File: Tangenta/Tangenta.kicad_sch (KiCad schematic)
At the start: 9 parts

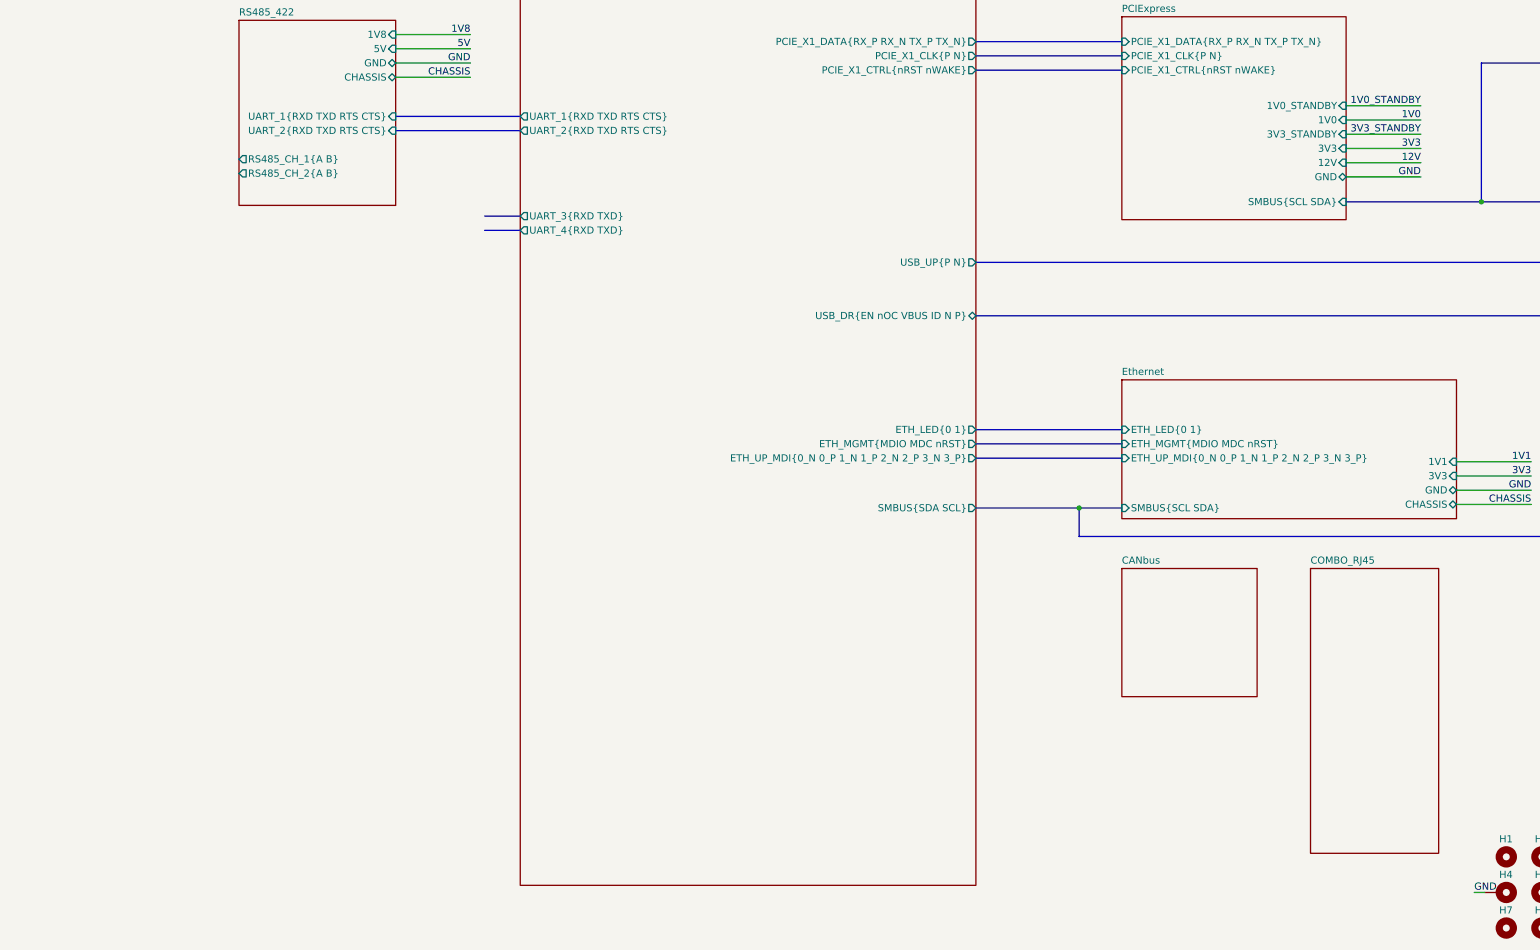
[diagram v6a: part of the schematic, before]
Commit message: Dual RS485 routed, done.
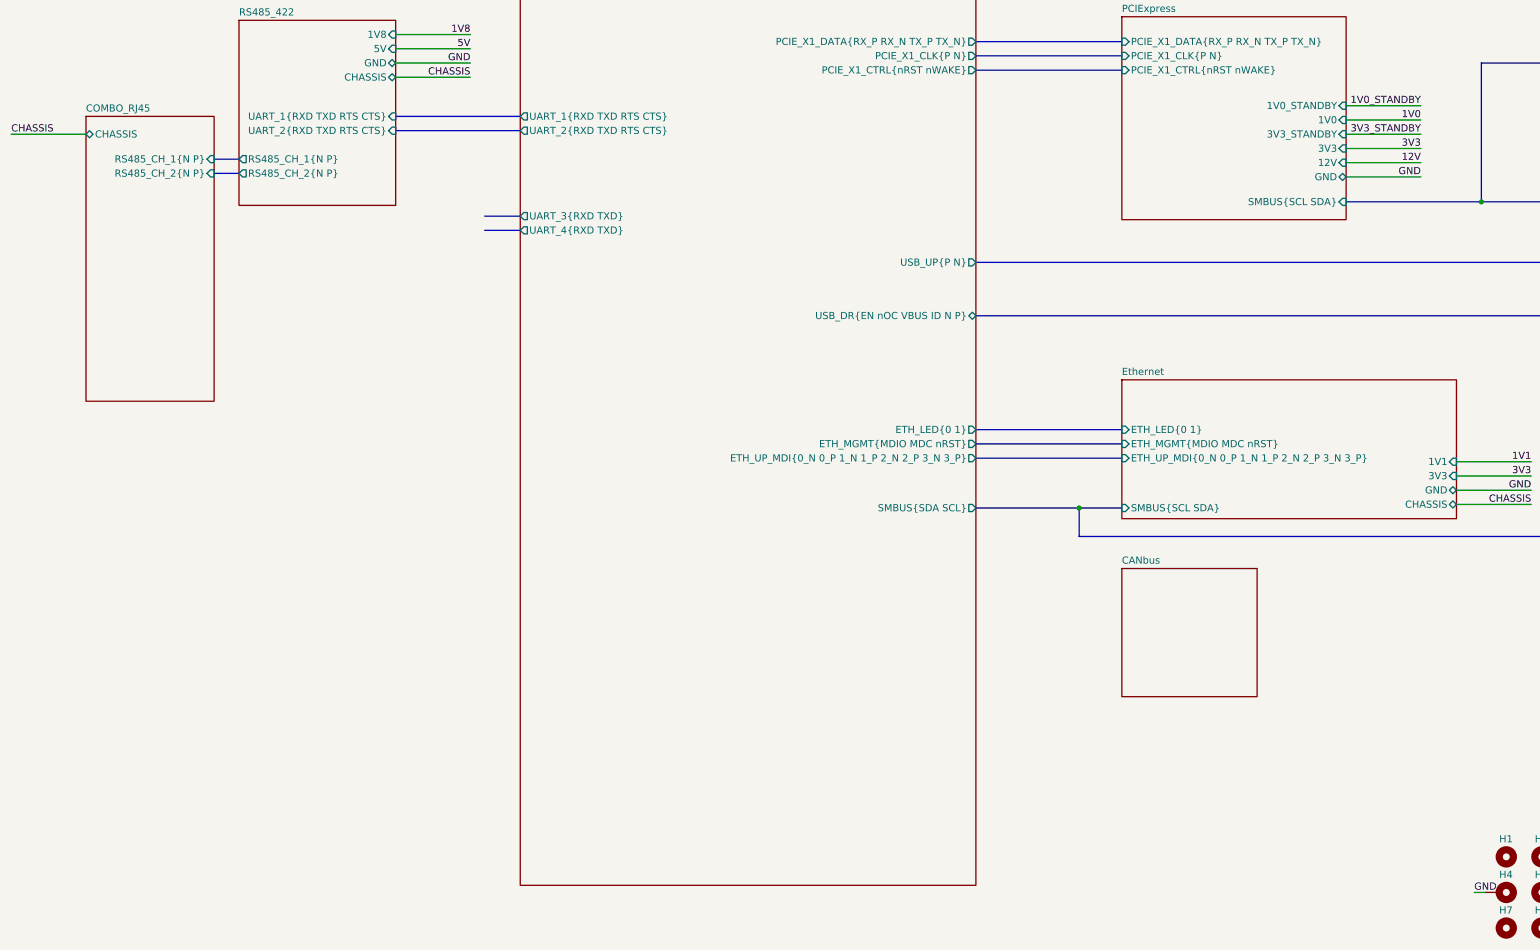
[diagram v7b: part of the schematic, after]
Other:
- sheet COMBO_RJ45 ports: added CHASSIS, RS485_CH_1{N P}, RS485_CH_2{N P}; removed none
- sheet RS485_422 ports: added RS485_CH_1{N P}, RS485_CH_2{N P}; removed RS485_CH_1{A B}, RS485_CH_2{A B}
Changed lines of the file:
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@@
+    (stroke (width 0) (type default))
+  )
+  (bus (pts (xy 52.705 145.415) (xy 57.15 145.415))
     (stroke (width 0) (type default))
   )
@@
     (stroke (width 0) (type default))
   )
+  (bus (pts (xy 52.705 142.875) (xy 57.15 142.875))
+    (stroke (width 0) (type default))
+  )
   (wire (pts (xy 333.375 184.785) (xy 346.71 184.785))
     (stroke (width 0) (type default))
   )
   (bus (pts (xy 207.01 205.105) (xy 214.63 205.105))
+    (stroke (width 0) (type default))
+  )
+  (wire (pts (xy 29.845 138.43) (xy 16.51 138.43))
     (stroke (width 0) (type default))
   )
@@
     (effects (font (size 1.27 1.27)) (justify right bottom))
   )
+  (label "CHASSIS" (at 16.51 138.43 0) (fields_autoplaced)
+    (effects (font (size 1.27 1.27)) (justify left bottom))
+  )
   (label "5V" (at 98.425 123.19 180) (fields_autoplaced)
     (effects (font (size 1.27 1.27)) (justify right bottom))
@@
       (effects (font (size 1.27 1.27)) (justify right))
     )
-    (pin "RS485_CH_1{A B}" output (at 57.15 142.875 180)
-      (effects (font (size 1.27 1.27)) (justify left))
-    )
-    (pin "RS485_CH_2{A B}" output (at 57.15 145.415 180)
+    (pin "RS485_CH_1{N P}" output (at 57.15 142.875 180)
+      (effects (font (size 1.27 1.27)) (justify left))
+    )
+    (pin "RS485_CH_2{N P}" output (at 57.15 145.415 180)
       (effects (font (size 1.27 1.27)) (justify left))
     )
@@
     )
   )
-  (sheet (at 248.285 215.9) (size 22.86 50.8) (fields_autoplaced)
-    (stroke (width 0.1524) (type solid))
-    (fill (color 0 0 0 0.0000))
-    (property "Sheetname" "COMBO_RJ45" (at 248.285 215.1884 0)
-      (effects (font (size 1.27 1.27)) (justify left bottom))
-    )
-    (property "Sheetfile" "COMBO_RJ45.kicad_sch" (at 248.285 267.2846 0)
-      (effects (font (size 1.27 1.27)) (justify left top) hide)
-    )
-    (instances
+  (sheet (at 29.845 135.255) (size 22.86 50.8) (fields_autoplaced)
+    (stroke (width 0.1524) (type solid))
+    (fill (color 0 0 0 0.0000))
+    (property "Sheetname" "COMBO_RJ45" (at 29.845 134.5434 0)
+      (effects (font (size 1.27 1.27)) (justify left bottom))
+    )
+    (property "Sheetfile" "COMBO_RJ45.kicad_sch" (at 29.845 186.6396 0)
+      (effects (font (size 1.27 1.27)) (justify left top) hide)
+    )
+    (pin "CHASSIS" bidirectional (at 29.845 138.43 180)
+      (effects (font (size 1.27 1.27)) (justify left))
+    )
+    (pin "RS485_CH_1{N P}" input (at 52.705 142.875 0)
+      (effects (font (size 1.27 1.27)) (justify right))
+    )
+    (pin "RS485_CH_2{N P}" input (at 52.705 145.415 0)
+      (effects (font (size 1.27 1.27)) (justify right))
+    )
+    (instances

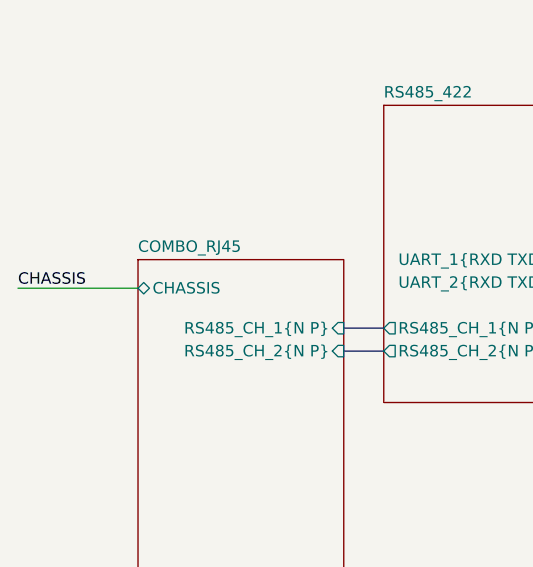
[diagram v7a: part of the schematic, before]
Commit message: Removing the old RS485 non-isolated transceivers.
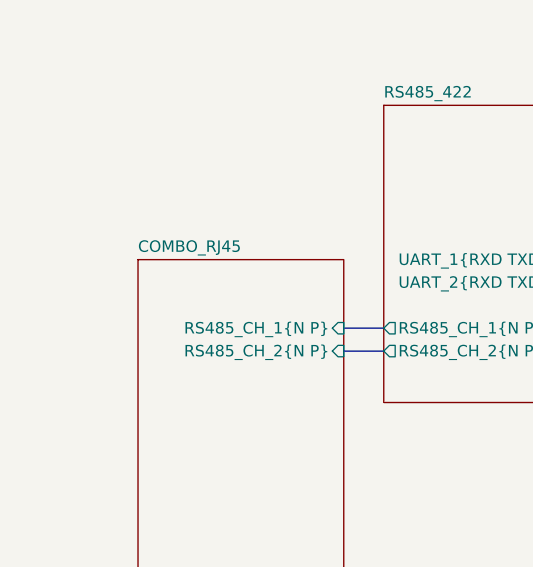
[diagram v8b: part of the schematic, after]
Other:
- sheet COMBO_RJ45 ports: added none; removed CHASSIS
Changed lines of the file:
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@@
-    (stroke (width 0) (type default))
-  )
-  (wire (pts (xy 29.845 138.43) (xy 16.51 138.43))
     (stroke (width 0) (type default))
   )
@@
     (effects (font (size 1.27 1.27)) (justify right bottom))
   )
-  (label "CHASSIS" (at 16.51 138.43 0) (fields_autoplaced)
-    (effects (font (size 1.27 1.27)) (justify left bottom))
-  )
   (label "5V" (at 98.425 123.19 180) (fields_autoplaced)
     (effects (font (size 1.27 1.27)) (justify right bottom))
@@
       (effects (font (size 1.27 1.27)) (justify left top) hide)
     )
-    (pin "CHASSIS" bidirectional (at 29.845 138.43 180)
-      (effects (font (size 1.27 1.27)) (justify left))
-    )
     (pin "RS485_CH_1{N P}" input (at 52.705 142.875 0)
